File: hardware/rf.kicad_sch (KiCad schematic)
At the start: 17 parts, among them IC6 SI4468-A2A-IMR, Y1 TG2520SMN_30.000M-MCGNNM0

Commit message: Done?
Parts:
- added C39, C40: 10n, Capacitor_SMD:C_0402_1005Metric, symbol Device:C
- added C41, C42, C45: 1n, Capacitor_SMD:C_0402_1005Metric, symbol Device:C
- added C43, C44, C46, C47: 8p8, Capacitor_SMD:C_0402_1005Metric, symbol Device:C
- added C48: 2u2, Capacitor_SMD:C_0805_2012Metric, symbol Device:C
- added C49: 100n, Capacitor_SMD:C_0805_2012Metric, symbol Device:C
- added C50: 100p, Capacitor_SMD:C_0603_1608Metric, symbol Device:C
- added C51: 33p, Capacitor_SMD:C_0402_1005Metric, symbol Device:C
- added C52: 100n, Capacitor_SMD:C_0402_1005Metric, symbol Device:C
- added D6, D7: BAR63-02L-E6327, BAR6302LE6327, symbol SamacSys_Parts:BAR63-02L-E6327
- added FB2: MMZ1608D241CTA00, SamacSys_Parts:BEADC1608X95N, symbol Device:FerriteBead_Small
- added J5: RFPC-SMA28-F, RFPCSMA28F, symbol SamacSys_Parts:RFPC-SMA28-F
- added L8, L9: 18n, LQW15CNR20J00B, symbol SamacSys_Parts:LQW15AN20NG00D
- added Q6: DMN1008UFDF-7, DMN1008UFDF7, symbol SamacSys_Parts:DMN1008UFDF-7
- added R34: 330 / 0, Resistor_SMD:R_0402_1005Metric, symbol Device:R
- added R35: 100k, Resistor_SMD:R_0402_1005Metric, symbol Device:R
- added R36, R37: 665, Resistor_SMD:R_0402_1005Metric, symbol Device:R
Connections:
- net 3V3 is gone; now on net +3V3: C32.1, R32.1, Y1.4 (VCC)
- net GND: now also IC6.1 (SDN), IC6.21 (GND_2), IC6.5 (NC), C39.1, C40.2, C43.2, C44.2, C46.2, C47.2, C48.2, C49.2, C50.2, C51.2, C52.2, D6.1 (K), J5.2, J5.3, J5.4, J5.5, Q6.4 (SOURCE_1), Q6.8 (SOURCE_2), R35.2
- net SW_Rx: now also C45.2
- net SW_Tx: now also C41.2
- net at FB1.1, R32.2: now also C39.2
- net COMMAND_DONE: now reaches IC6.10 (GPIO1)
- net nIRQ: now reaches IC6.11 (NIRQ)
- net SCLK: now reaches IC6.12 (SCLK)
- net SDO: now reaches IC6.13 (SDO)
- net SDI: now reaches IC6.14 (SDI)
- net nSEL: now reaches IC6.15 (NSEL)
- net SW_MOS: now reaches IC6.20 (GPIO3)
- net SW_MOS: now also R35.1, R36.1, R37.2
- net +3V3: now reaches IC6.6 (VDD_1)
- net +3V3: now also IC6.8 (VDD_2), C48.1, C49.1, C50.1, C51.1, C52.1
- new net: Q6.3 (GATE), R36.2
- new net: C47.1, J5.1, L9.2
- new net: C44.1, C45.1, D6.2 (A), L8.2
- new net: C42.2, C43.1, D7.1 (K), L8.1
- new net: C41.1, D7.2 (A), FB2.2
- new net: C40.1, FB2.1, R34.2
- new net ANT: C42.1, C46.1, L9.1
- new net SW: Q6.1 (DRAIN_1), Q6.2 (DRAIN_2), Q6.5 (DRAIN_3), Q6.6 (DRAIN_4), Q6.7 (DRAIN_5), R34.1, R37.1
- no-connect marks 1 -> 4
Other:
- note added: "<"
- note added: "Antenna connector"
- note added: "Connect GPIO to switch directly, if current higher than 5 mA is not required"
- note added: "Limit current to 5mA max."
- note added: "MOSFET switch to enable higher currents for PIN diodes"
- note added: "Power supply"
- note added: "Pull down to initiate SPI communication"
- note added: "Pulls down when sending interrupt"
- note added: "Pulls up, when the last command was completed or is ready to receive SPI commands after boot"
- note added: "Separate from the board's reference ground plane"
- note added: "Switch"
- note added: "To avoid shut-down mode"
- note added: "To limit current to 10 mA. Solder jumper instead, if MOSFET was not used"
- note added: "V"
- note added: "^"
- moved on the sheet: C32, C33, C34, C35, C36, C37, C38, FB1, IC6, L2, L3, L4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

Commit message: 0R added to RF supply
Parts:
- added R38: 0, symbol Device:R
- R34: footprint Resistor_SMD:R_0402_1005Metric -> Resistor_SMD:R_0603_1608Metric
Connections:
- net +3V3: now also R38.1; no longer C52.1, IC6.8 (VDD_2)
- new net VDD2: C52.1, IC6.8 (VDD_2), R38.2
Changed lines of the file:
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@@
 	(paper "A4")
 	(junction
+		(at 273.05 20.32)
+		(diameter 0)
+		(color 0 0 0 0)
+	)
+	(junction
 		(at 55.88 138.43)
 		(diameter 0)
@@
 	)
 	(junction
-		(at 234.95 20.32)
-		(diameter 0)
-		(color 0 0 0 0)
-	)
-	(junction
 		(at 234.95 50.8)
 		(diameter 0)
@@
 	)
 	(junction
-		(at 273.05 20.32)
-		(diameter 0)
-		(color 0 0 0 0)
-	)
-	(junction
 		(at 171.45 142.24)
 		(diameter 0)
@@
 		(color 0 0 0 0)
 	)
+	(junction
+		(at 234.95 20.32)
+		(diameter 0)
+		(color 0 0 0 0)
+	)
 	(no_connect
 		(at 204.47 128.27)
@@
 	(wire
 		(pts
-			(xy 234.95 20.32) (xy 234.95 40.64)
-		)
-		(stroke
-			(width 0)
-			(type default)
-		)
-	)
-	(wire
-		(pts
 			(xy 260.35 41.91) (xy 260.35 40.64)
 		)
@@
 	(wire
 		(pts
+			(xy 234.95 20.32) (xy 250.19 20.32)
+		)
+		(stroke
+			(width 0)
+			(type default)
+		)
+	)
+	(wire
+		(pts
 			(xy 273.05 20.32) (xy 279.4 20.32)
 		)
@@
 	(wire
 		(pts
+			(xy 257.81 20.32) (xy 273.05 20.32)
+		)
+		(stroke
+			(width 0)
+			(type default)
+		)
+	)
+	(wire
+		(pts
 			(xy 234.95 50.8) (xy 247.65 50.8)
 		)
@@
 	(wire
 		(pts
+			(xy 234.95 20.32) (xy 234.95 40.64)
+		)
+		(stroke
+			(width 0)
+			(type default)
+		)
+	)
+	(wire
+		(pts
 			(xy 31.75 156.21) (xy 31.75 167.64)
 		)
@@
 	(wire
 		(pts
-			(xy 234.95 20.32) (xy 273.05 20.32)
-		)
-		(stroke
-			(width 0)
-			(type default)
-		)
-	)
-	(wire
-		(pts
 			(xy 125.73 165.1) (xy 140.97 165.1)
 		)
@@
 	)
 	(symbol
+		(lib_id "Device:R")
+		(at 254 20.32 90)
+		(unit 1)
+		(exclude_from_sim no)
+		(in_bom yes)
+		(on_board yes)
+		(dnp no)
+		(property "Reference" "R38"
+			(at 254 24.638 90)
+			(effects
+				(font
+					(size 1.27 1.27)
+				)
+			)
+		)
+		(property "Value" "0"
+			(at 254 27.178 90)
+			(effects
+				(font
+					(size 1.27 1.27)
+				)
+			)
+		)
+		(property "Footprint" ""
+			(at 254 22.098 90)
+			(effects
+				(font
+					(size 1.27 1.27)
+				)
+				(hide yes)
+			)
+		)
+		(property "Datasheet" "~"
+			(at 254 20.32 0)
+			(effects
+				(font
+					(size 1.27 1.27)
+				)
+				(hide yes)
+			)
+		)
+		(property "Description" "Resistor"
+			(at 254 20.32 0)
+			(effects
+				(font
+					(size 1.27 1.27)
+				)
+				(hide yes)
+			)
+		)
+		(pin "2"
+		)
+		(pin "1"
+		)
+		(instances
+			(project ""
+				(path "/e8e834c4-1afb-42f7-b718-3cb720dae1d5/21633f2b-133b-44f0-ac2e-c32a8c0675be"
+					(reference "R38")
+					(unit 1)
+				)
+			)
+		)
+	)
+	(symbol
 		(lib_id "Device:C")
 		(at 100.33 46.99 180)
@@
 			)
 		)
-		(property "Footprint" "Resistor_SMD:R_0402_1005Metric"
+		(property "Footprint" "Resistor_SMD:R_0603_1608Metric"
 			(at 93.98 136.652 90)
 			(effects

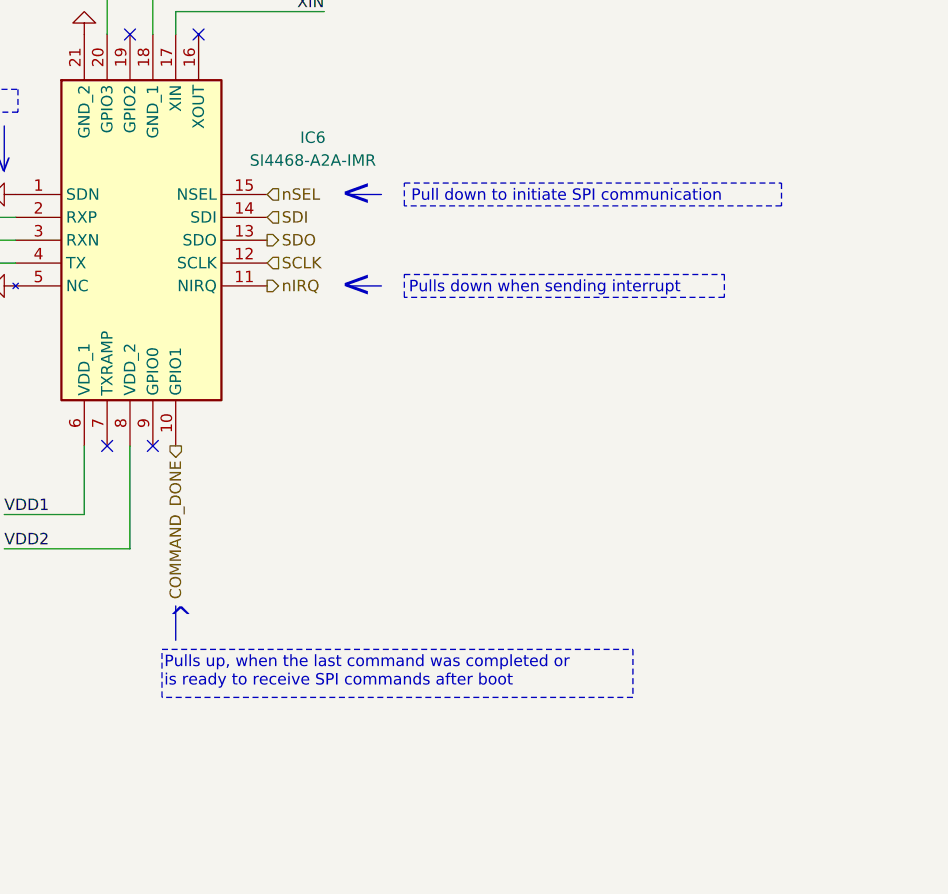
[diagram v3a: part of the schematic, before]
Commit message: Board connector added
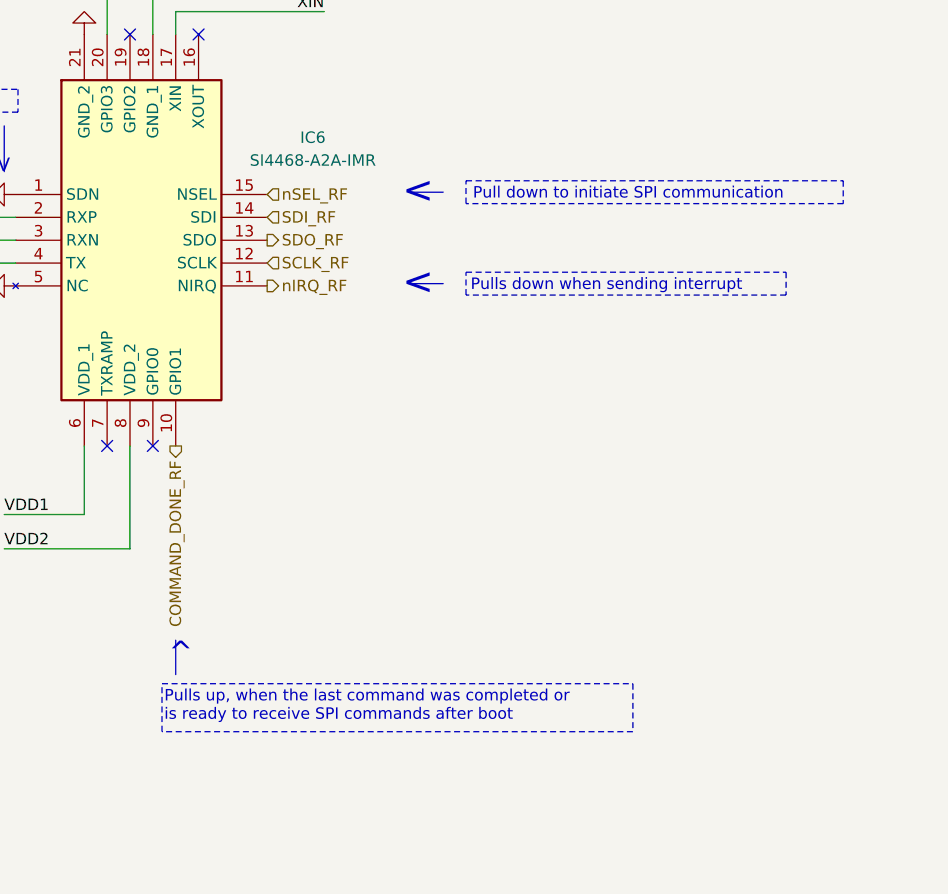
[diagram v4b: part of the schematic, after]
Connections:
- net COMMAND_DONE renamed COMMAND_DONE_RF
- net SCLK renamed SCLK_RF
- net SDI renamed SDI_RF
- net SDO renamed SDO_RF
- net nIRQ renamed nIRQ_RF
- net nSEL renamed nSEL_RF
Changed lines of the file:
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@@
 	(polyline
 		(pts
-			(xy 226.06 110.49) (xy 229.87 110.49)
+			(xy 232.918 110.236) (xy 236.728 110.236)
 		)
 		(stroke
@@
 	(polyline
 		(pts
-			(xy 226.06 100.33) (xy 229.87 100.33)
+			(xy 232.918 100.076) (xy 236.728 100.076)
 		)
 		(stroke
@@
 	(polyline
 		(pts
-			(xy 207.01 146.05) (xy 207.01 149.86)
+			(xy 207.01 149.86) (xy 207.01 153.67)
 		)
 		(stroke
@@
 	)
 	(rectangle
-		(start 205.486 150.876)
-		(end 257.81 156.21)
+		(start 205.486 154.686)
+		(end 257.81 160.02)
 		(stroke
 			(width 0)
@@
 	)
 	(rectangle
-		(start 232.41 109.22)
-		(end 267.97 111.76)
+		(start 239.268 108.966)
+		(end 274.828 111.506)
 		(stroke
 			(width 0)
@@
 	)
 	(rectangle
-		(start 232.41 99.06)
-		(end 274.32 101.6)
+		(start 239.268 98.806)
+		(end 281.178 101.346)
 		(stroke
 			(width 0)
@@
 	(text "Pulls up, when the last command was completed or\nis ready to receive SPI commands after boot"
 		(exclude_from_sim no)
-		(at 205.74 153.416 0)
+		(at 205.74 157.226 0)
 		(effects
 			(font
@@
 	(text "<"
 		(exclude_from_sim no)
-		(at 227.076 100.33 0)
+		(at 233.934 100.076 0)
 		(effects
 			(font
@@
 	(text "Pulls down when sending interrupt"
 		(exclude_from_sim no)
-		(at 232.918 110.744 0)
+		(at 239.776 110.49 0)
 		(effects
 			(font
@@
 	(text "^"
 		(exclude_from_sim no)
-		(at 206.248 147.574 0)
+		(at 206.248 151.384 0)
 		(effects
 			(font
@@
 	(text "Pull down to initiate SPI communication"
 		(exclude_from_sim no)
-		(at 233.172 100.584 0)
+		(at 240.03 100.33 0)
 		(effects
 			(font
@@
 	(text "<"
 		(exclude_from_sim no)
-		(at 227.076 110.49 0)
+		(at 233.934 110.236 0)
 		(effects
 			(font
@@
 		)
 	)
-	(hierarchical_label "SDO"
+	(hierarchical_label "SDO_RF"
 		(shape output)
 		(at 217.17 105.41 0)
@@
 		)
 	)
-	(hierarchical_label "COMMAND_DONE"
+	(hierarchical_label "COMMAND_DONE_RF"
 		(shape output)
 		(at 207.01 128.27 270)
@@
 		)
 	)
-	(hierarchical_label "SDI"
+	(hierarchical_label "SDI_RF"
 		(shape input)
 		(at 217.17 102.87 0)
@@
 		)
 	)
-	(hierarchical_label "nIRQ"
+	(hierarchical_label "nIRQ_RF"
 		(shape output)
 		(at 217.17 110.49 0)
@@
 		)
 	)
-	(hierarchical_label "nSEL"
+	(hierarchical_label "nSEL_RF"
 		(shape input)
 		(at 217.17 100.33 0)
@@
 		)
 	)
-	(hierarchical_label "SCLK"
+	(hierarchical_label "SCLK_RF"
 		(shape input)
 		(at 217.17 107.95 0)

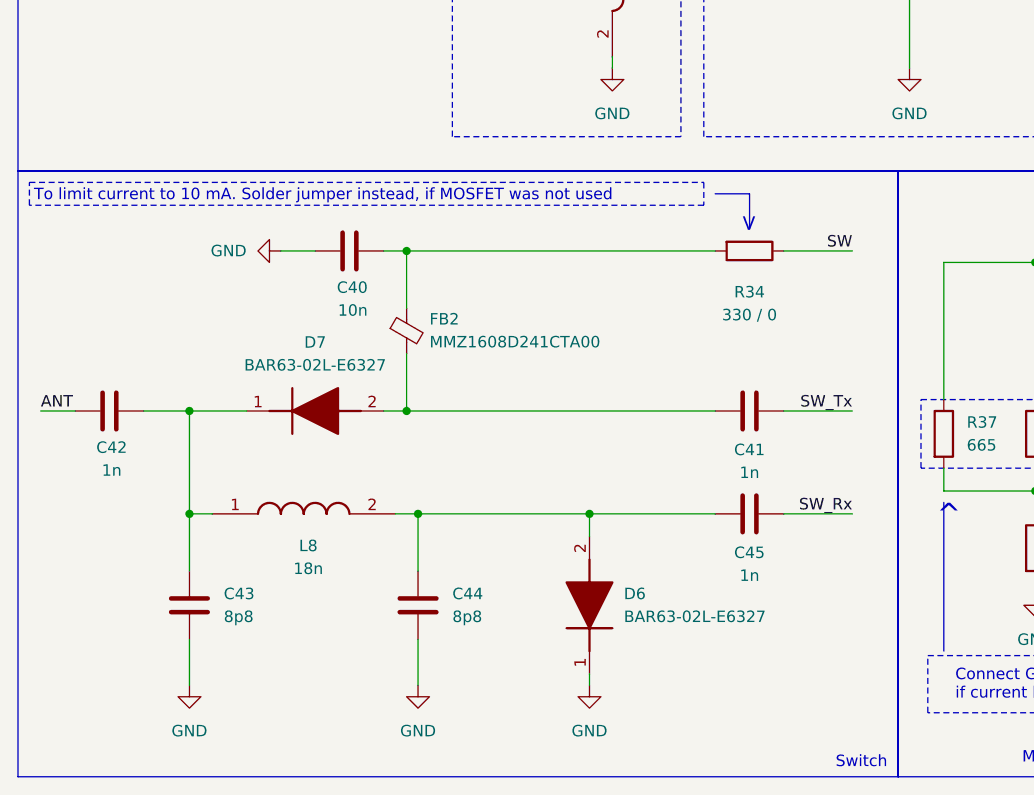
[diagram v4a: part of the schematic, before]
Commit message: Fixed MOS and board connector
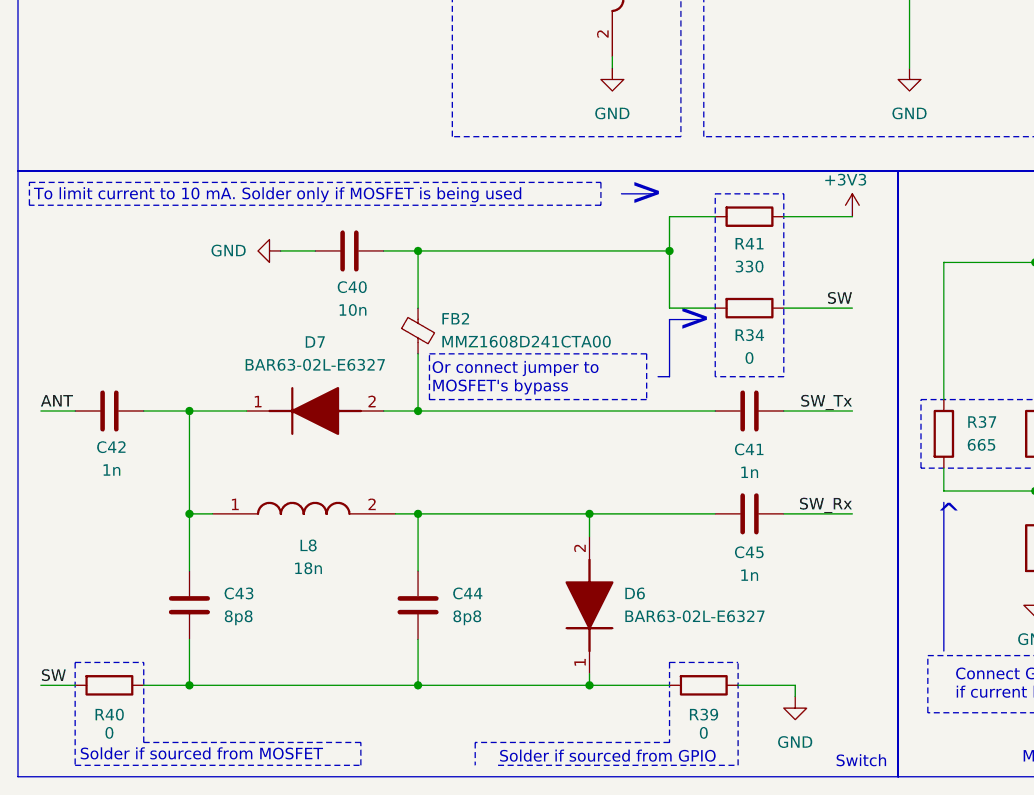
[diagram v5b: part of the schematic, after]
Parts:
- added R39, R40: 0, Resistor_SMD:R_0603_1608Metric, symbol Device:R
- added R41: 330, Resistor_SMD:R_0603_1608Metric, symbol Device:R
- R34: value 330 / 0 -> 0
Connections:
- net +3V3: now also R41.1
- net GND: now also R39.1; no longer C43.2, C44.2, D6.1 (K)
- net SW: now also R40.2
- net at C40.1, FB2.1, R34.2: now also R41.2
- new net: C43.2, C44.2, D6.1 (K), R39.2, R40.1
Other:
- note added: ">"
- note added: "Or connect jumper to MOSFET's bypass"
- note added: "Solder if sourced from GPIO"
- note added: "Solder if sourced from MOSFET"
- note added: "To limit current to 10 mA. Solder only if MOSFET is being used"
- note removed: "To limit current to 10 mA. Solder jumper instead, if MOSFET was not used"
- moved on the sheet: FB2

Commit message: Revised and completed BOM
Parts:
- R23: renamed from R38; footprint (none) -> Resistor_SMD:R_0603_1608Metric
- renumbered C32 to C16, C33 to C17, C38 to C18, C37 to C19, C46 to C20, C47 to C21, C52 to C22, C48 to C23, C49 to C24, C50 to C25, C51 to C26, C39 to C27, C34 to C28, C35 to C29, C36 to C30, C40 to C31, C42 to C32, C41 to C33, C43 to C34, C44 to C35, C45 to C36, D7 to D6, D6 to D7, IC6 to IC8, L6 to L2, L7 to L3, L9 to L4, L2 to L5, L3 to L6, L4 to L7, L5 to L8, L8 to L9, R32 to R24, R41 to R25, R34 to R26, R40 to R27, R39 to R28, R37 to R29, R36 to R30, R35 to R31, Y1 to TCXO
